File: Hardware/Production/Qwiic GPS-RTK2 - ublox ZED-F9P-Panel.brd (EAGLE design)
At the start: 160.8 x 100.6 mm, 807 parts, among them J1 Radio, J11 U.FL, J13 U.FL, J16 Radio, J18 PTH, J20 U.FL, J24 Radio, J26 PTH, J28 U.FL, J3 PTH, J32 Radio, J34 PTH, J36 U.FL, J40 Radio, J42 PTH, J44 U.FL, J48 Radio, J9 PTH, U1 3.3V, U10 ZED-F9P, U11 3.3V, U12 ZED-F9P, U2 3.3V, U3 ZED-F9P, U4 ZED-F9P, U5 3.3V, U6 ZED-F9P, U7 3.3V, U8 ZED-F9P, U9 3.3V

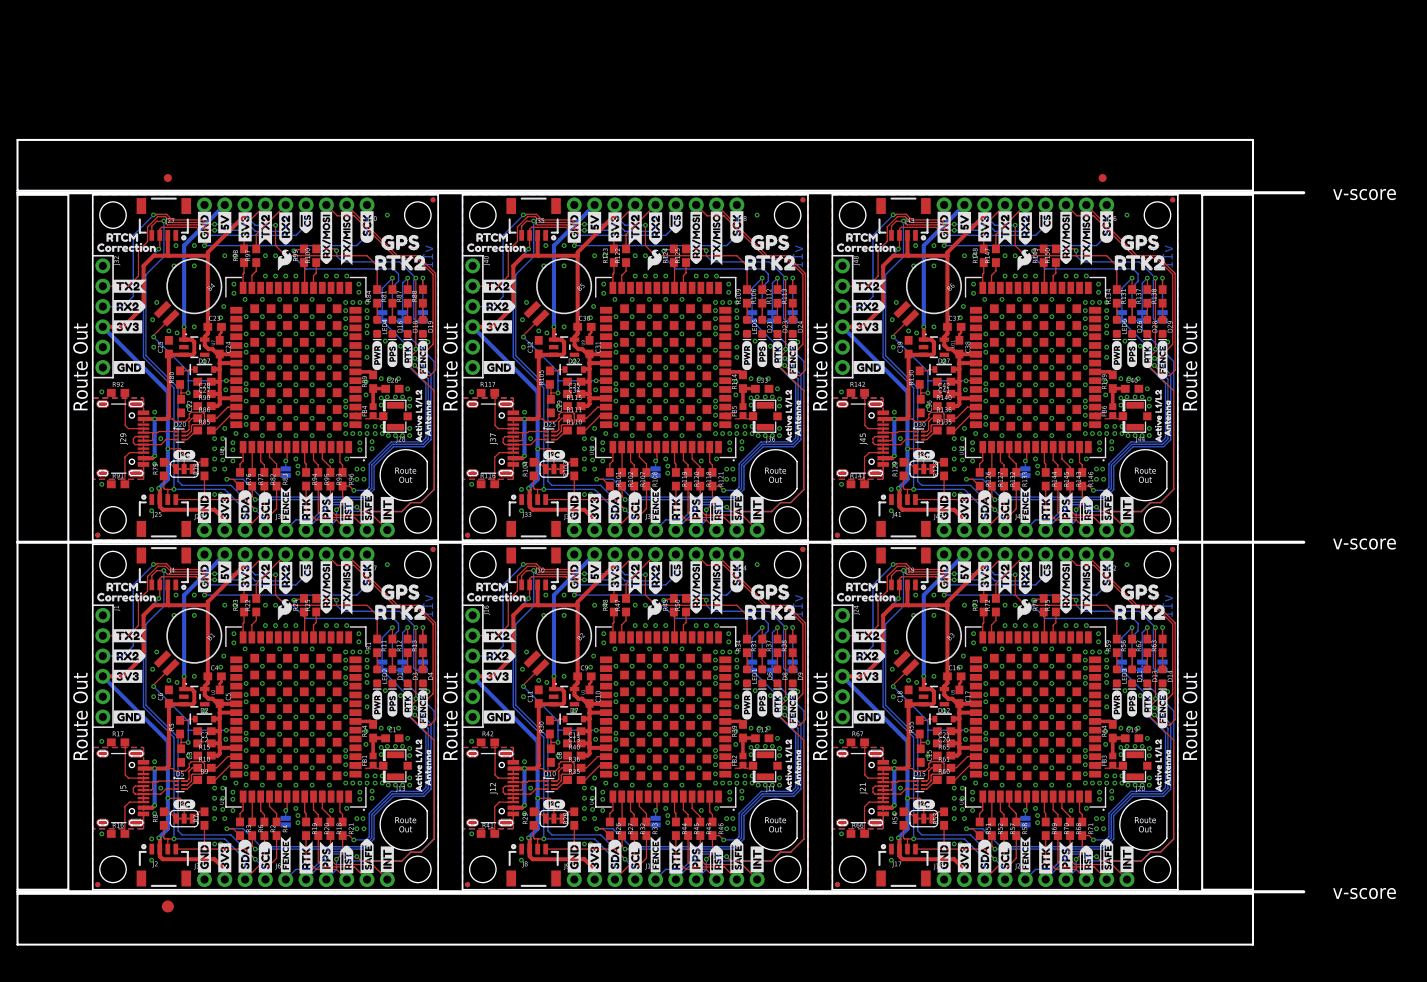
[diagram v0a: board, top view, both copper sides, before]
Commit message: Adds panel for v20
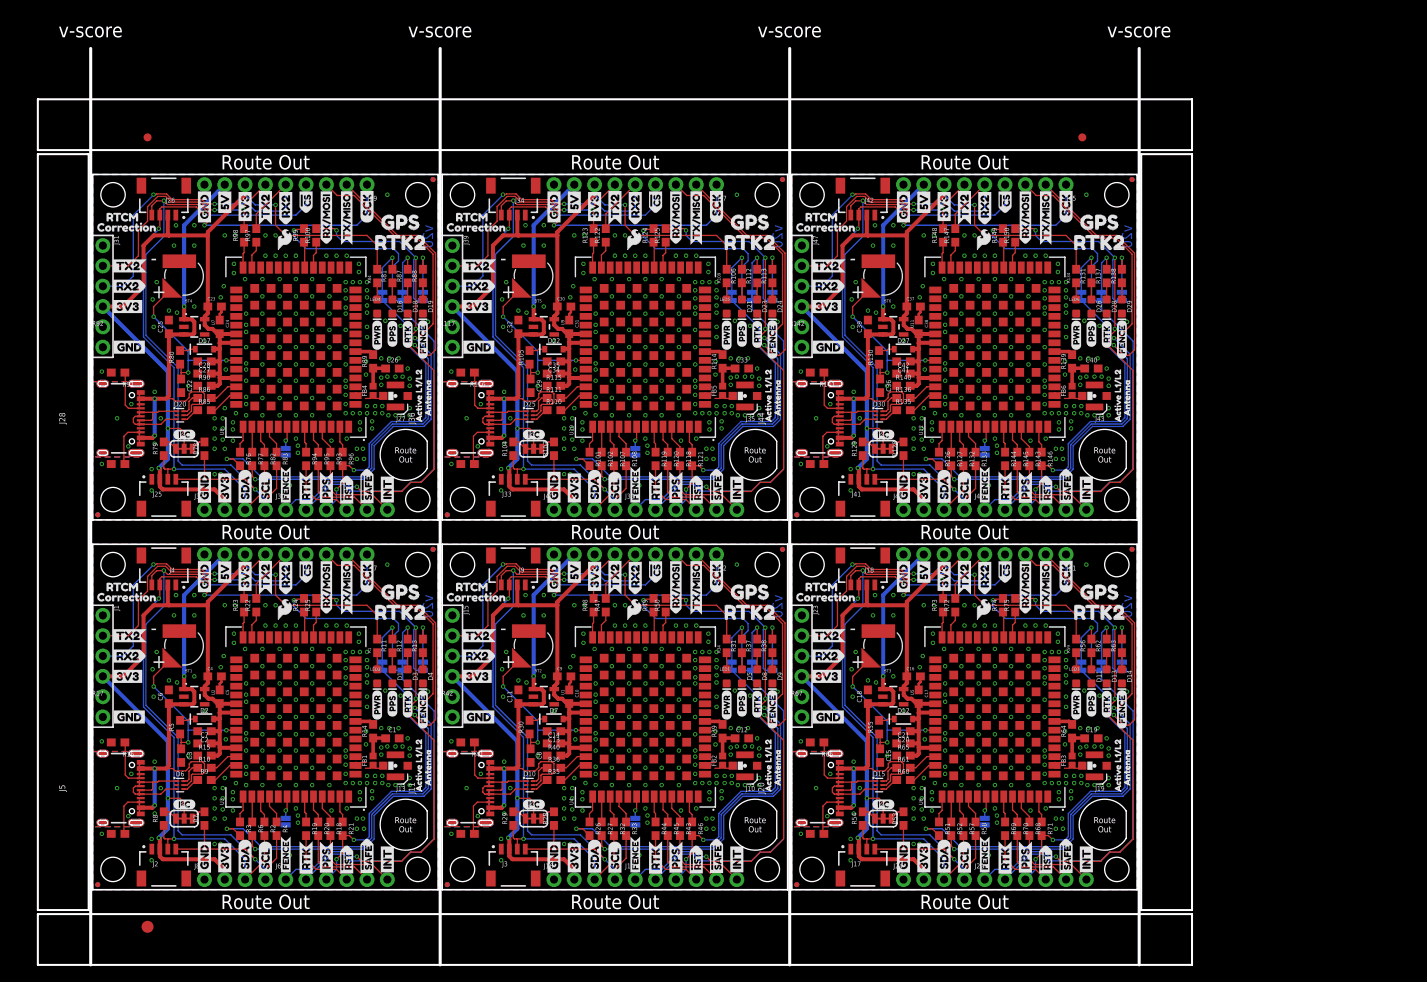
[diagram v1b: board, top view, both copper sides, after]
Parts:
- removed B1, B2, B3, B4, B5, B6: 6.8MM_COIN_CELL, SparkFun-Batteries:BATTCON-6.8MM
- added BT1, BT2, BT3, BT4, BT5, BT6: ML414H_IV01E_BATTERY, SparkFun-Batteries:ML414H_IV01E
- D10, D15, D20, D25, D30: device funbit:SOT886 -> SparkFun-IC-Power:SOT886
- D5: value PRTR5V0U2F -> Yellow; device funbit:SOT886 -> SparkFun-LED:LED-0603
- D6: value Yellow -> PRTR5V0U2F; device SparkFun-LED:LED-0603 -> SparkFun-IC-Power:SOT886
- J10, J19, J27, J35, J43: value (none) -> U.FL; device SparkFun-Connectors:1X04_1MM_RA -> SparkFun-Connectors:U.FL
- J11, J20, J28, J36, J44: value U.FL -> (none); device SparkFun-Connectors:U.FL -> SparkFun-Connectors:USB-C-16P
- J12, J21, J29, J37, J45: device USB-C:USB-C-16P -> SparkFun-Connectors:1X09_NO_SILK
- J14, J22, J30, J38, J46: device SparkFun-Connectors:1X09_NO_SILK -> SparkFun-Connectors:1X06_NO_SILK
- J15, J23, J31, J39, J47: value (none) -> Radio
- J16, J24, J32, J40, J48: value Radio -> (none); device SparkFun-Connectors:1X06_NO_SILK -> SparkFun-Connectors:1X04_NO_SILK
- J17, J2, J25, J33, J4, J41: value (none) -> Qwiic Right Angle; device SparkFun-Connectors:1X04_1MM_RA -> SparkFun-Connectors:JST04_1MM_RA
- J18, J26, J3, J34, J42, J9: value PTH -> Qwiic Right Angle; device SparkX:1X04_NO_SILK -> SparkFun-Connectors:JST04_1MM_RA
- J5: device USB-C:USB-C-16P -> SparkFun-Connectors:USB-C-16P
- J8: device SparkFun-Connectors:1X04_1MM_RA -> SparkFun-Connectors:1X04_NO_SILK
- JP1, JP11, JP17, JP18, JP2, JP25, JP3, JP32, JP33, JP39, JP46, JP47, JP53, JP59, JP60, JP67, JP74, JP75: value (none) -> JUMPER-SMT_2_NC_TRACE_SILK
- JP10, JP24, JP38, JP5, JP52, JP66: value (none) -> JUMPER-SMT_3_2-NC_TRACE_SILK
- JP101, JP14, JP15, JP19, JP20, JP28, JP29, JP31, JP34, JP35, JP41, JP43, JP44, JP48, JP49, JP56, JP57, JP6, JP62, JP63, JP7, JP70, JP72, JP91: value STAND-OFF -> STAND-OFFTIGHT; device SparkFun:STAND-OFF -> SparkFun-Hardware:STAND-OFF-TIGHT
- JP12, JP13, JP21, JP22, JP23, JP26, JP27, JP36, JP37, JP40, JP42, JP50, JP51, JP54, JP55, JP61, JP64, JP65, JP68, JP69, JP71, JP8, JP81, JP9: device SparkFun:MICRO-FIDUCIAL -> SparkFun-Aesthetics:FIDUCIAL-MICRO
- JP16, JP30, JP4, JP45, JP58, JP73: value (none) -> JUMPER-SMT_2_NO_SILK
- U10, U12, U3, U4, U6, U8: device ZED-F9P:ZED-F9P -> SparkFun-GPS:ZED-F9P
- moved D6 74.0 mm to (10.9, 13.1), turned to 0 degrees
- moved D5 71.5 mm to (81.2, 26.7), turned to 270 degrees
- moved J47 45.2 mm to (88.6, 80.5), turned to 270 degrees
- moved J39 43.7 mm to (45.0, 80.5), turned to 270 degrees
- moved J22 43.4 mm to (111.5, 1.27), turned to 0 degrees
- moved J23 43.3 mm to (88.6, 34.3), turned to 270 degrees
- moved J14 42.6 mm to (67.8, 1.27), turned to 0 degrees
- moved J29 42.3 mm to (34.3, 88.1), turned to 180 degrees
- moved J31 42.3 mm to (1.27, 80.5), turned to 270 degrees
- moved J15 41.7 mm to (45.0, 34.3), turned to 270 degrees
- moved J8 41.3 mm to (14.0, 1.27)
- moved J46 41.0 mm to (111.5, 47.5), turned to 0 degrees
- moved J42 40.7 mm to (96.3, 84.3), turned to 180 degrees
- moved J37 40.7 mm to (78.0, 88.1), turned to 180 degrees
- moved J38 40.2 mm to (67.8, 47.5), turned to 0 degrees
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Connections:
- net !RESET1: now also J14.4; no longer J15.4
- net !RESET2: now also J22.4; no longer J23.4
- net !RESET3: now also J30.4; no longer J31.4
- net !RESET4: now also J38.4; no longer J39.4
- net !RESET5: now also J46.4; no longer J47.4
- net !SAFE1: now also J14.5; no longer J15.5
- net !SAFE2: now also J22.5; no longer J23.5
- net !SAFE3: now also J30.5; no longer J31.5
- net !SAFE4: now also J38.5; no longer J39.5
- net !SAFE5: now also J46.5; no longer J47.5
- net 3.3V: now also J8.2; no longer J3.2
- net 3.3V1: now also J12.7, J15.4, J16.2, J3.2; no longer J10.2, J14.7, J16.4, J8.2
- net 3.3V2: now also J21.7, J23.4, J24.2; no longer J19.2, J22.7, J24.4
- net 3.3V3: now also J29.7, J31.4, J32.2; no longer J27.2, J30.7, J32.4
- net 3.3V4: now also J37.7, J39.4, J40.2; no longer J35.2, J38.7, J40.4
- net 3.3V5: now also J45.7, J47.4, J48.2; no longer J43.2, J46.7, J48.4
- net 5V: now also D6.5; no longer D5.5
- net 5V1: now also J11.VBUS1, J11.VBUS2, J12.8; no longer J12.VBUS1, J12.VBUS2, J14.8
- net 5V2: now also J20.VBUS1, J20.VBUS2, J21.8; no longer J21.VBUS1, J21.VBUS2, J22.8
- net 5V3: now also J28.VBUS1, J28.VBUS2, J29.8; no longer J29.VBUS1, J29.VBUS2, J30.8
- net 5V4: now also J36.VBUS1, J36.VBUS2, J37.8; no longer J37.VBUS1, J37.VBUS2, J38.8
- net 5V5: now also J44.VBUS1, J44.VBUS2, J45.8; no longer J45.VBUS1, J45.VBUS2, J46.8
- net BACKUP: now also BT1.+; no longer B1.+
- net BACKUP1: now also BT2.+; no longer B2.+
- net BACKUP2: now also BT3.+; no longer B3.+
- net BACKUP3: now also BT4.+; no longer B4.+
- net BACKUP4: now also BT5.+; no longer B5.+
- net BACKUP5: now also BT6.+; no longer B6.+
- net CC10: now also J36.B5; no longer J37.B5
- net CC11: now also J44.A5; no longer J45.A5
- net CC12: now also J44.B5; no longer J45.B5
- net CC3: now also J11.A5; no longer J12.A5
- net CC4: now also J11.B5; no longer J12.B5
- net CC5: now also J20.A5; no longer J21.A5
- net CC6: now also J20.B5; no longer J21.B5
- net CC7: now also J28.A5; no longer J29.A5
- net CC8: now also J28.B5; no longer J29.B5
- net CC9: now also J36.A5; no longer J37.A5
- net D+: now also D6.4; no longer D5.4
- net D-: now also D6.6; no longer D5.6
- net FENCE_STAT1: now also J14.1; no longer J15.1
- net FENCE_STAT2: now also J22.1; no longer J23.1
- net FENCE_STAT3: now also J30.1; no longer J31.1
- net FENCE_STAT4: now also J38.1; no longer J39.1
- net FENCE_STAT5: now also J46.1; no longer J47.1
- net GND: now also BT1.-, D6.2, J8.1; no longer B1.-, D5.2, J3.1
- net GND1: now also BT2.-, D5.C, J10.2, J11.GND, J11.GND2, J12.9, J15.6, J16.1, J3.1; no longer B2.-, D6.C, J11.1, J11.2, J12.GND, J12.GND2, J14.9, J16.6, J8.1
- net GND2: now also BT3.-, J19.2, J20.GND, J20.GND2, J21.9, J23.6, J24.1; no longer B3.-, J20.1, J20.2, J21.GND, J21.GND2, J22.9, J24.6
- net GND3: now also BT4.-, J27.2, J28.GND, J28.GND2, J29.9, J31.6, J32.1; no longer B4.-, J28.1, J28.2, J29.GND, J29.GND2, J30.9, J32.6
- net GND4: now also BT5.-, J35.2, J36.GND, J36.GND2, J37.9, J39.6, J40.1; no longer B5.-, J36.1, J36.2, J37.GND, J37.GND2, J38.9, J40.6
- net GND5: now also BT6.-, J43.2, J44.GND, J44.GND2, J45.9, J47.6, J48.1; no longer B6.-, J44.1, J44.2, J45.GND, J45.GND2, J46.9, J48.6
- net GPS_ANT2: now also J10.FEED; no longer J11.FEED
- net GPS_ANT3: now also J19.FEED; no longer J20.FEED
- net GPS_ANT4: now also J27.FEED; no longer J28.FEED
- net GPS_ANT5: now also J35.FEED; no longer J36.FEED
- net GPS_ANT6: now also J43.FEED; no longer J44.FEED
- net INT1: now also J14.6; no longer J15.6
- net INT2: now also J22.6; no longer J23.6
- net INT3: now also J30.6; no longer J31.6
- net INT4: now also J38.6; no longer J39.6
- net INT5: now also J46.6; no longer J47.6
- net N$23: now also D5.A; no longer D6.A
- net PPS1: now also J14.3; no longer J15.3
- net PPS2: now also J22.3; no longer J23.3
- net PPS3: now also J30.3; no longer J31.3
- net PPS4: now also J38.3; no longer J39.3
- net PPS5: now also J46.3; no longer J47.3
- net RTK_STAT1: now also J14.2; no longer J15.2
- net RTK_STAT2: now also J22.2; no longer J23.2
- net RTK_STAT3: now also J30.2; no longer J31.2
- net RTK_STAT4: now also J38.2; no longer J39.2
- net RTK_STAT5: now also J46.2; no longer J47.2
- net RX1: now also J12.5, J15.3; no longer J14.5, J16.3
- net RX3: now also J21.5, J23.3; no longer J22.5, J24.3
- net RX4: now also J29.5, J31.3; no longer J30.5, J32.3
- net RX5: now also J37.5, J39.3; no longer J38.5, J40.3
- net RX6: now also J45.5, J47.3; no longer J46.5, J48.3
- net RXI/MOSI1: now also J12.3; no longer J14.3
- net RXI/MOSI2: now also J21.3; no longer J22.3
- net RXI/MOSI3: now also J29.3; no longer J30.3
- net RXI/MOSI4: now also J37.3; no longer J38.3
- net RXI/MOSI5: now also J45.3; no longer J46.3
- net SCL/SCK: now also J8.4; no longer J3.4
- net SCL/SCK1: now also J12.1, J16.4, J3.4; no longer J10.4, J14.1, J8.4
- net SCL/SCK2: now also J21.1, J24.4; no longer J19.4, J22.1
- net SCL/SCK3: now also J29.1, J32.4; no longer J27.4, J30.1
- net SCL/SCK4: now also J37.1, J40.4; no longer J35.4, J38.1
- net SCL/SCK5: now also J45.1, J48.4; no longer J43.4, J46.1
- net SDA/!CS: now also J8.3; no longer J3.3
- net SDA/!CS1: now also J12.4, J16.3, J3.3; no longer J10.3, J14.4, J8.3
- net SDA/!CS2: now also J21.4, J24.3; no longer J19.3, J22.4
- net SDA/!CS3: now also J29.4, J32.3; no longer J27.3, J30.4
- net SDA/!CS4: now also J37.4, J40.3; no longer J35.3, J38.4
- net SDA/!CS5: now also J45.4, J48.3; no longer J43.3, J46.4
- net SHLD1: now also J11.SHLD1, J11.SHLD2, J11.SHLD3, J11.SHLD4, J11.SHLD5, J11.SHLD6, J11.SHLD7, J11.SHLD8; no longer J12.SHLD1, J12.SHLD2, J12.SHLD3, J12.SHLD4, J12.SHLD5, J12.SHLD6, J12.SHLD7, J12.SHLD8
- net SHLD2: now also J20.SHLD1, J20.SHLD2, J20.SHLD3, J20.SHLD4, J20.SHLD5, J20.SHLD6, J20.SHLD7, J20.SHLD8; no longer J21.SHLD1, J21.SHLD2, J21.SHLD3, J21.SHLD4, J21.SHLD5, J21.SHLD6, J21.SHLD7, J21.SHLD8
- net SHLD3: now also J28.SHLD1, J28.SHLD2, J28.SHLD3, J28.SHLD4, J28.SHLD5, J28.SHLD6, J28.SHLD7, J28.SHLD8; no longer J29.SHLD1, J29.SHLD2, J29.SHLD3, J29.SHLD4, J29.SHLD5, J29.SHLD6, J29.SHLD7, J29.SHLD8
- net SHLD4: now also J36.SHLD1, J36.SHLD2, J36.SHLD3, J36.SHLD4, J36.SHLD5, J36.SHLD6, J36.SHLD7, J36.SHLD8; no longer J37.SHLD1, J37.SHLD2, J37.SHLD3, J37.SHLD4, J37.SHLD5, J37.SHLD6, J37.SHLD7, J37.SHLD8
- net SHLD5: now also J44.SHLD1, J44.SHLD2, J44.SHLD3, J44.SHLD4, J44.SHLD5, J44.SHLD6, J44.SHLD7, J44.SHLD8; no longer J45.SHLD1, J45.SHLD2, J45.SHLD3, J45.SHLD4, J45.SHLD5, J45.SHLD6, J45.SHLD7, J45.SHLD8
- net TX1: now also J12.6, J15.2; no longer J14.6, J16.2
- net TX3: now also J21.6, J23.2; no longer J22.6, J24.2
- net TX4: now also J29.6, J31.2; no longer J30.6, J32.2
- net TX5: now also J37.6, J39.2; no longer J38.6, J40.2
- net TX6: now also J45.6, J47.2; no longer J46.6, J48.2
- net TXO/MISO1: now also J12.2; no longer J14.2
- net TXO/MISO2: now also J21.2; no longer J22.2
- net TXO/MISO3: now also J29.2; no longer J30.2
- net TXO/MISO4: now also J37.2; no longer J38.2
- net TXO/MISO5: now also J45.2; no longer J46.2
- net UNP_D+: now also D6.3; no longer D5.3
- net UNP_D+1: now also J11.A6, J11.B6; no longer J12.A6, J12.B6
- net UNP_D+2: now also J20.A6, J20.B6; no longer J21.A6, J21.B6
- net UNP_D+3: now also J28.A6, J28.B6; no longer J29.A6, J29.B6
- net UNP_D+4: now also J36.A6, J36.B6; no longer J37.A6, J37.B6
- net UNP_D+5: now also J44.A6, J44.B6; no longer J45.A6, J45.B6
- net UNP_D-: now also D6.1; no longer D5.1
- net UNP_D-1: now also J11.A7, J11.B7; no longer J12.A7, J12.B7
- net UNP_D-2: now also J20.A7, J20.B7; no longer J21.A7, J21.B7
- net UNP_D-3: now also J28.A7, J28.B7; no longer J29.A7, J29.B7
- net UNP_D-4: now also J36.A7, J36.B7; no longer J37.A7, J37.B7
- net UNP_D-5: now also J44.A7, J44.B7; no longer J45.A7, J45.B7
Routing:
- net UNP_D-5: track 6.29 -> 6.97 mm
- net UNP_D-4: track 6.29 -> 6.97 mm
- net UNP_D-2: track 6.29 -> 6.97 mm
- net UNP_D-1: track 6.29 -> 6.97 mm
- net 5V2: track 52.8 -> 53.5 mm
- net 5V1: track 52.8 -> 53.5 mm
- net UNP_D-3: track 6.29 -> 6.97 mm
- net UNP_D-: track 6.29 -> 6.97 mm
- net 5V: track 52.8 -> 53.5 mm
- net 5V5: track 52.8 -> 53.5 mm
- net 5V4: track 52.8 -> 53.5 mm
- net 5V3: track 52.8 -> 53.5 mm
- net BACKUP4: track 20.9 -> 21.4 mm
- net BACKUP1: track 20.9 -> 21.4 mm
- net BACKUP: track 20.9 -> 21.4 mm
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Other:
- board size 160.8 x 100.6 mm -> 144.3 x 114.6 mm
- board text added: "+"
- board text added: "-"
- board text added: "v20"
- board text removed: "v11"
